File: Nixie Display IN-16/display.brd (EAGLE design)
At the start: 112.6 x 51.6 mm, 22 parts, among them U1 TPIC6B595DWRG4, U2 TPIC6B595DWRG4, U3 TPIC6B595DWRG4, U4 TPIC6B595DWRG4, U5 TPIC6B595DWRG4, X1 22-23-2021

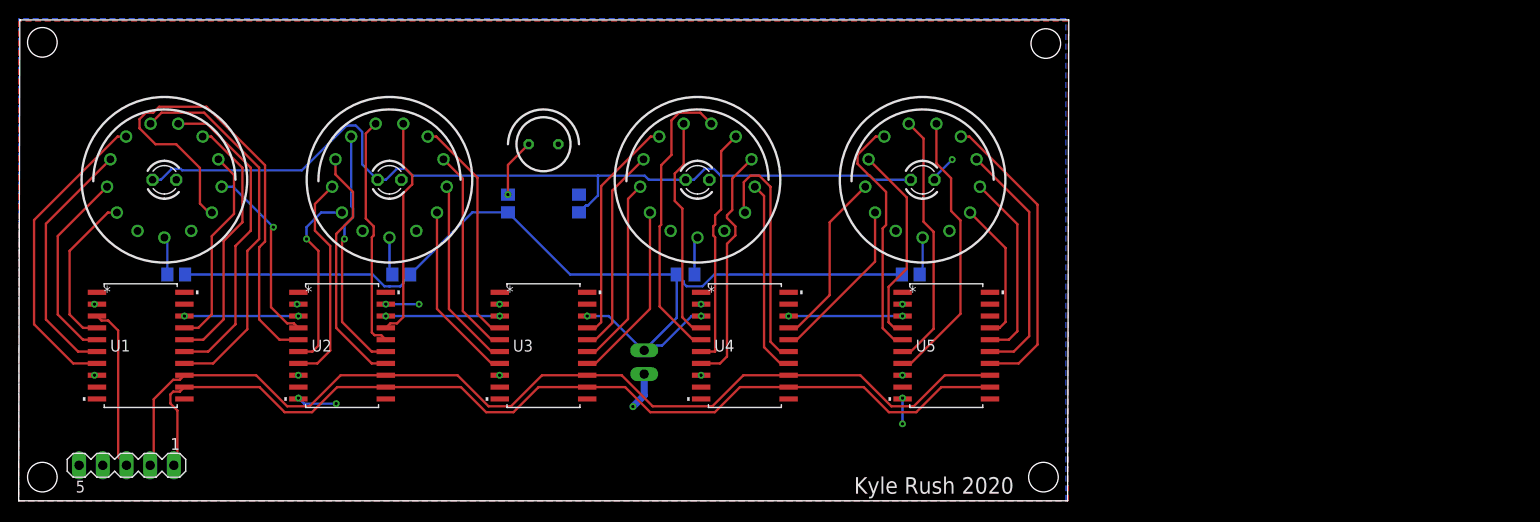
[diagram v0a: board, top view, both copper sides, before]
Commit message: Tweaks design, adds arduino clock sketch
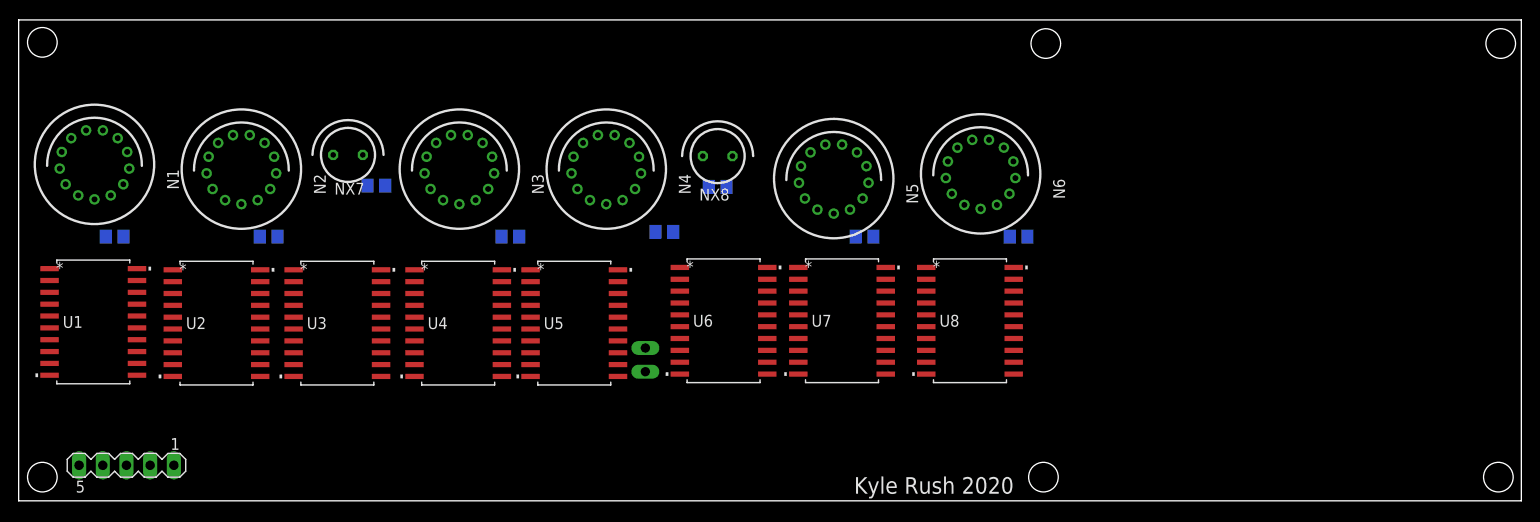
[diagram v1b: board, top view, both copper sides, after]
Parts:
- removed LED1, LED2, LED3, LED4: (no value), led:LED3MM
- added N6: IN-16, nixies-us:IN-16
- added NX7, NX8: IN-3, nixies-us:IN-3
- added R7, R8: 68k, rcl:R0805
- added U6, U7, U8: TPIC6B595DWRG4, Digikey:DW20
- N1, N2, N3, N4: value IN-14 -> IN-16; device nixies-us:IN-14 -> nixies-us:IN-16
- N5: value IN-3 -> IN-16; device nixies-us:IN-3 -> nixies-us:IN-16
- R1: value 330 -> 15k
- R2: value 68k -> 15k
- moved R1 49.9 mm to (10.3, 28.3), turned to 180 degrees
- moved U5 40.0 mm to (59.6, 19.1)
- moved R3 36.0 mm to (52.7, 28.3), turned to 0 degrees
- moved N4 33.9 mm to (63.0, 35.6)
- moved N5 31.3 mm to (87.4, 34.5)
- moved U4 30.8 mm to (47.1, 19.1)
- moved R4 28.6 mm to (69.2, 28.8), turned to 0 degrees
- moved R2 25.9 mm to (26.8, 28.3), turned to 180 degrees
- moved N3 25.6 mm to (47.2, 35.6)
- moved U3 22.2 mm to (34.2, 19.1)
- moved R5 19.6 mm to (90.7, 28.3)
- moved N2 15.9 mm to (23.9, 35.6)
- moved U2 13.7 mm to (21.2, 19.1)
- moved R6 12.3 mm to (107.2, 28.3)
- moved N1 7.67 mm to (8.13, 36.1)
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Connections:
- removed net N$21: LED1.A, LED2.A, LED3.A, LED4.A, R1.1
- new net N$50: U5.18, U6.3
- new net N$51: N5.A, R5.1
- new net N$53: N6.A, R6.1
- new net N$56: N5.0, U7.5
- new net N$57: N5.7, U6.16
- new net N$58: N5.6, U6.15
- new net N$59: N5.5, U6.14
- new net N$60: N5.4, U6.7
- new net N$61: N5.3, U6.6
- new net N$62: N5.2, U6.5
- new net N$63: N5.1, U6.4
- new net N$64: U6.18, U7.3
- new net N$67: N5.8, U6.17
- new net N$68: N5.9, U7.4
- new net N$69: U7.18, U8.3
- new net N$72: N6.1, U7.6
- new net N$73: N6.2, U7.7
- new net N$74: N6.3, U7.14
- new net N$75: N6.4, U7.15
- new net N$76: N6.5, U7.16
- new net N$80: N6.6, U7.17
- new net N$81: N6.7, U8.4
- new net N$82: N6.8, U8.5
- new net N$83: N6.9, U8.6
- new net N$84: N6.0, U8.7
- new net N$85: NX8.A, R8.2
- new net N$88: NX7.K, U8.14
- new net N$89: NX8.K, U8.15
- net GND: now also U6.10, U6.11, U6.19, U6.9, U7.10, U7.11, U7.19, U7.9, U8.10, U8.11, U8.19, U8.9; no longer LED1.K, LED2.K, LED3.K, LED4.K, N5.K
- net N$22: now also NX7.A, R7.2; no longer N5.A, R2.2
- net N$23: now also R1.1; no longer R3.1
- net N$24: now also R2.1; no longer R4.1
- net N$25: now also R3.1; no longer R5.1
- net N$26: now also R4.1; no longer R6.1
- net N$28: now also U6.12, U7.12, U8.12
- net N$49: now also U6.13, U7.13, U8.13
- net V+: now also R1.2, R2.2, R7.1, R8.1; no longer R2.1
- net VCC: now also U6.2, U6.8, U7.2, U7.8, U8.2, U8.8; no longer R1.2
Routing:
- net N$49: track 109.0 -> 0.00 mm
- net N$28: track 105.2 -> 0.00 mm
- net N$21: track 95.1 -> 0.00 mm
- net V+: track 94.3 -> 0.00 mm
- net N$10: track 53.2 -> 0.00 mm
- net N$5: track 40.7 -> 0.00 mm
- net N$6: track 33.9 -> 0.00 mm
- net N$4: track 33.2 -> 0.00 mm
- net N$44: track 32.2 -> 0.00 mm
- net N$34: track 31.5 -> 0.00 mm
- net N$45: track 29.9 -> 0.00 mm
- net N$7: track 27.8 -> 0.00 mm
- net N$46: track 27.4 -> 0.00 mm
- net N$3: track 26.9 -> 0.00 mm
- net N$13: track 26.5 -> 0.00 mm
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- removed copper zone on layer 1, net GND
- removed copper zone on layer 16, net VCC
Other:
- board size 112.6 x 51.6 mm -> 161.1 x 51.6 mm
